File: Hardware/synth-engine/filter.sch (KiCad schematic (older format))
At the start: 36 parts, among them J6 AUDIO-JACK4-.25-HORIZ-TRS, U4 TL074CN, U5 SSI2144

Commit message: add separate PCB with potentiometers and switches and connector between control board and synth engine
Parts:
- U4: footprint SparkFun-AnalogIC:SOIC8 -> SparkFun-AnalogIC:SO16
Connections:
- net at J6.RING (RING-NORM): now also J6.TIP, RV17.2
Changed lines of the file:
@@
 $Descr A4 11693 8268
 encoding utf-8
-Sheet 4 6
+Sheet 4 7
 Title ""
 Date ""
@@
 F 0 "U4" H 8050 3800 60  0000 L CNN
 F 1 "TL074CN" H 8050 3550 60  0000 L CNN
-F 2 "SparkFun-AnalogIC:SOIC8" H 8150 3900 60  0001 L CNN
+F 2 "SparkFun-AnalogIC:SO16" H 8150 3900 60  0001 L CNN
 F 3 "http://www.ti.com/lit/ds/symlink/tl071a.pdf" H 8150 4000 60  0001 L CNN
 F 4 "296-1777-5-ND" H 8150 4100 60  0001 L CNN "Digi-Key_PN"
@@
 F 0 "U4" H 3900 4400 60  0000 L CNN
 F 1 "TL074CN" H 3900 4150 60  0000 L CNN
-F 2 "SparkFun-AnalogIC:SOIC8" H 4000 4500 60  0001 L CNN
+F 2 "SparkFun-AnalogIC:SO16" H 4000 4500 60  0001 L CNN
 F 3 "http://www.ti.com/lit/ds/symlink/tl071a.pdf" H 4000 4600 60  0001 L CNN
 F 4 "296-1777-5-ND" H 4000 4700 60  0001 L CNN "Digi-Key_PN"

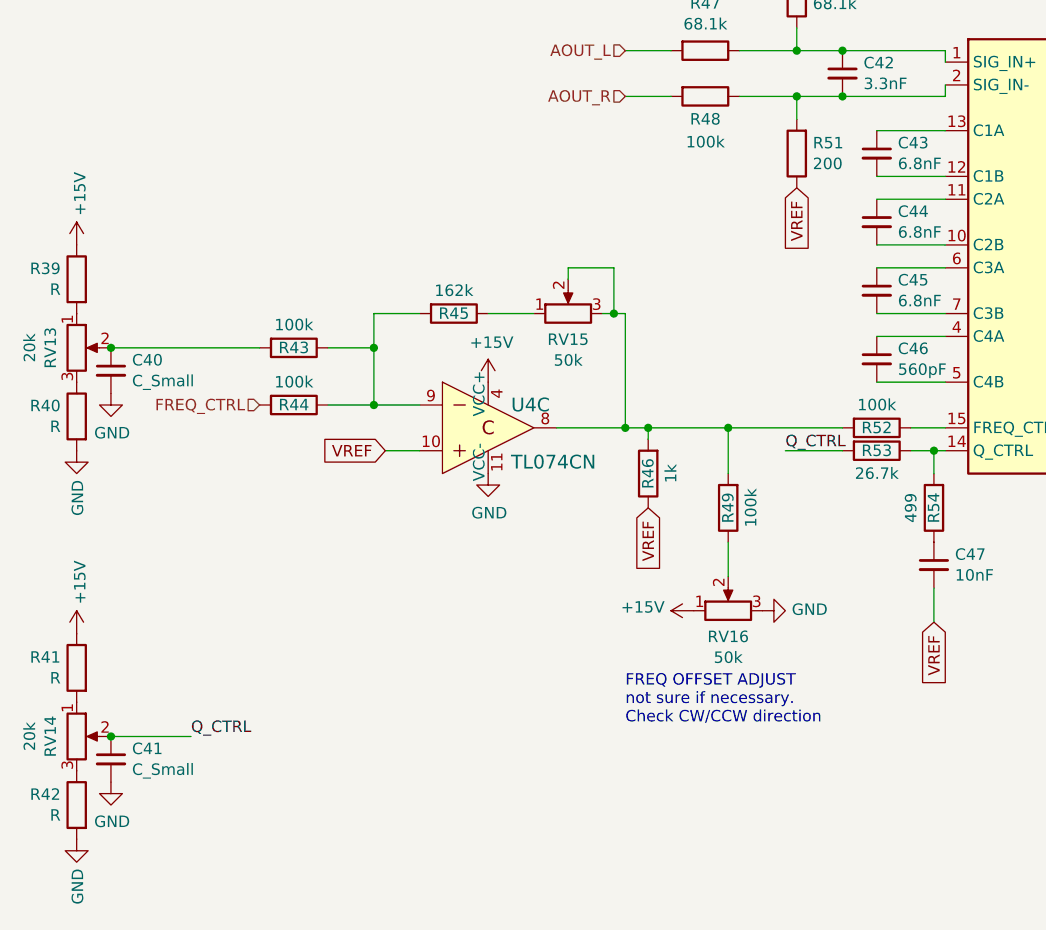
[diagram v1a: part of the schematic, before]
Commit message: initial routing complete. Still need to do ground plane pours. There are still some issues with incorrect footprints.
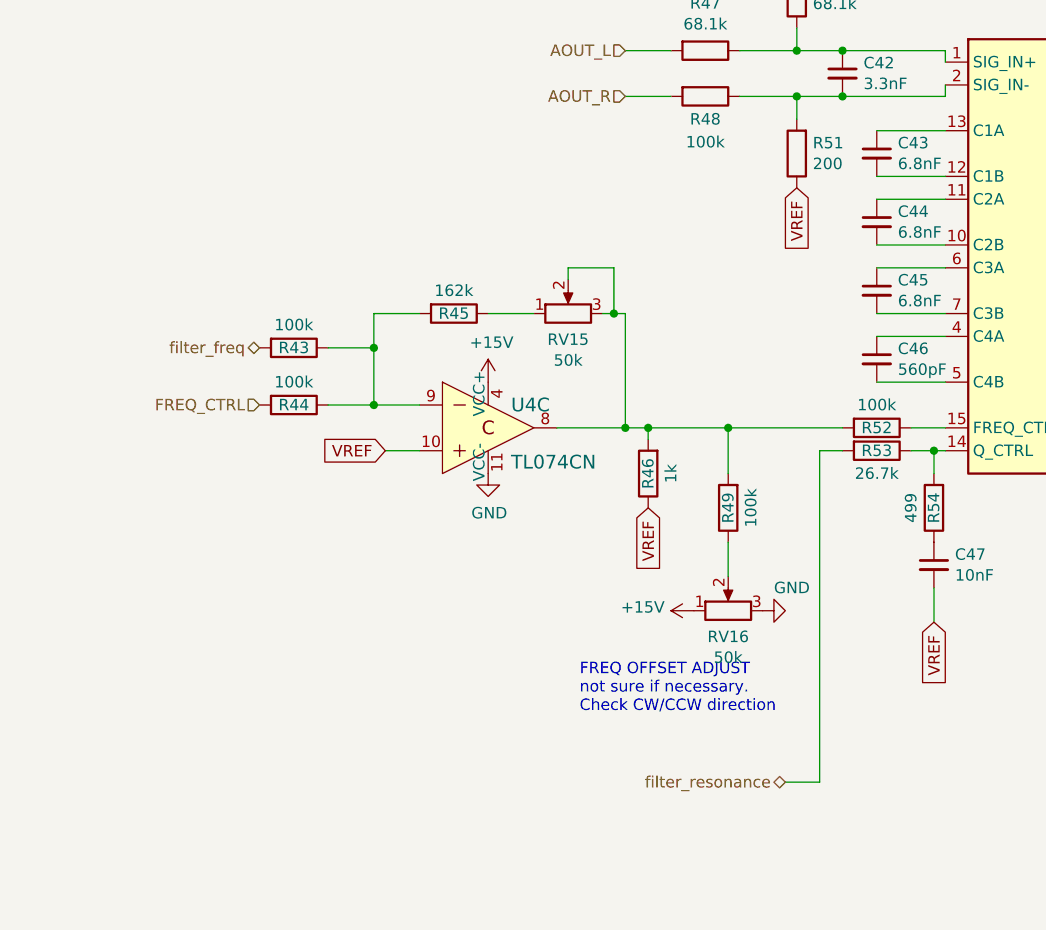
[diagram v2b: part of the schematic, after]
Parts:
- removed C40, C41: C_Small, SparkFun-Passives:0805, symbol Device:C_Small
- removed R39, R40, R41, R42: R, SparkFun-Passives:0805, symbol Device:R
- removed RV13, RV14: 20k, Potentiometer_THT:Potentiometer_Alps_RK09K_Single_Vertical, symbol Device:R_POT
- RV15, RV16: footprint Potentiometer_THT:Potentiometer_Alps_RK09K_Single_Vertical -> SparkFun-Electromechanical:TRIMPOT-3MM-2
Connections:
- net filter_freq: now reaches R43.2
- net at J6.RING (RING-NORM): now also J6.TIP, RV17.2
- net Q_CTRL renamed filter_resonance
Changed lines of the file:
@@
 P 5000 5100
 F 0 "#PWR069" H 5000 4850 50  0001 C CNN
-F 1 "GND" V 5005 4972 50  0000 R CNN
+F 1 "GND" V 5100 5050 50  0000 R CNN
 F 2 "" H 5000 5100 50  0001 C CNN
 F 3 "" H 5000 5100 50  0001 C CNN
@@
 	0    -1   -1   0
 $EndComp
-Text Notes 4400 5600 0    50   ~ 0
+Text Notes 4200 5550 0    50   ~ 0
 FREQ OFFSET ADJUST\nnot sure if necessary.\nCheck CW/CCW direction
 $Comp
@@
 F 0 "RV16" V 4736 5100 50  0000 C CNN
 F 1 "50k" V 4645 5100 50  0000 C CNN
-F 2 "Potentiometer_THT:Potentiometer_Alps_RK09K_Single_Vertical" H 4850 5100 50  0001 C CNN
+F 2 "SparkFun-Electromechanical:TRIMPOT-3MM-2" H 4850 5100 50  0001 C CNN
 F 3 "~" H 4850 5100 50  0001 C CNN
 	1    4850 5100
@@
 F 0 "RV15" V 4036 3800 50  0000 C CNN
 F 1 "50k" V 3945 3800 50  0000 C CNN
-F 2 "Potentiometer_THT:Potentiometer_Alps_RK09K_Single_Vertical" H 4150 3800 50  0001 C CNN
+F 2 "SparkFun-Electromechanical:TRIMPOT-3MM-2" H 4150 3800 50  0001 C CNN
 F 3 "~" H 4150 3800 50  0001 C CNN
 	1    4150 3800
@@
 	1    0    0    -1
 $EndComp
-Text Label 5100 4400 0    50   ~ 0
-Q_CTRL
-Wire Wire Line
-	5100 4400 5350 4400
 Text GLabel 5750 5150 3    50   Input ~ 0
 VREF
@@
 $EndComp
 $Comp
-L power:+15V #PWR060
-U 1 1 5DDC8B0C
-P 2000 3500
-F 0 "#PWR060" H 2000 3350 50  0001 C CNN
-F 1 "+15V" V 2015 3628 50  0000 L CNN
-F 2 "" H 2000 3500 50  0001 C CNN
-F 3 "" H 2000 3500 50  0001 C CNN
-	1    2000 3500
-	1    0    0    -1
-$EndComp
-$Comp
-L power:GND #PWR061
-U 1 1 5DDC8B12
-P 2000 4400
-F 0 "#PWR061" H 2000 4150 50  0001 C CNN
-F 1 "GND" V 2005 4272 50  0000 R CNN
-F 2 "" H 2000 4400 50  0001 C CNN
-F 3 "" H 2000 4400 50  0001 C CNN
-	1    2000 4400
-	1    0    0    -1
-$EndComp
-$Comp
-L Device:R_POT RV13
-U 1 1 5DDC8B18
-P 2000 3950
-F 0 "RV13" V 1886 3950 50  0000 C CNN
-F 1 "20k" V 1795 3950 50  0000 C CNN
-F 2 "Potentiometer_THT:Potentiometer_Alps_RK09K_Single_Vertical" H 2000 3950 50  0001 C CNN
-F 3 "~" H 2000 3950 50  0001 C CNN
-	1    2000 3950
-	1    0    0    -1
-$EndComp
-Wire Wire Line
-	2150 3950 2800 3950
-$Comp
-L Device:R R40
-U 1 1 5DDD4D4F
-P 2000 4250
-F 0 "R40" H 2070 4296 50  0000 L CNN
-F 1 "R" H 2070 4205 50  0000 L CNN
-F 2 "SparkFun-Passives:0805" V 1930 4250 50  0001 C CNN
-F 3 "~" H 2000 4250 50  0001 C CNN
-	1    2000 4250
-	-1   0    0    -1
-$EndComp
-$Comp
-L Device:R R39
-U 1 1 5DDD7C21
-P 2000 3650
-F 0 "R39" H 2070 3696 50  0000 L CNN
-F 1 "R" H 2070 3605 50  0000 L CNN
-F 2 "SparkFun-Passives:0805" V 1930 3650 50  0001 C CNN
-F 3 "~" H 2000 3650 50  0001 C CNN
-	1    2000 3650
-	-1   0    0    -1
-$EndComp
-$Comp
-L Device:C_Small C40
-U 1 1 5DDDB3D4
-P 2150 4050
-F 0 "C40" H 2242 4096 50  0000 L CNN
-F 1 "C_Small" H 2242 4005 50  0000 L CNN
-F 2 "SparkFun-Passives:0805" H 2150 4050 50  0001 C CNN
-F 3 "~" H 2150 4050 50  0001 C CNN
-	1    2150 4050
-	1    0    0    -1
-$EndComp
-Connection ~ 2150 3950
-$Comp
-L power:GND #PWR064
-U 1 1 5DDDB4EF
-P 2150 4150
-F 0 "#PWR064" H 2150 3900 50  0001 C CNN
-F 1 "GND" H 2155 3977 50  0000 C CNN
-F 2 "" H 2150 4150 50  0001 C CNN
-F 3 "" H 2150 4150 50  0001 C CNN
-	1    2150 4150
-	1    0    0    -1
-$EndComp
-$Comp
-L power:+15V #PWR062
-U 1 1 5DDE1C9A
-P 2000 5200
-F 0 "#PWR062" H 2000 5050 50  0001 C CNN
-F 1 "+15V" V 2015 5328 50  0000 L CNN
-F 2 "" H 2000 5200 50  0001 C CNN
-F 3 "" H 2000 5200 50  0001 C CNN
-	1    2000 5200
-	1    0    0    -1
-$EndComp
-$Comp
-L power:GND #PWR063
-U 1 1 5DDE1CA0
-P 2000 6100
-F 0 "#PWR063" H 2000 5850 50  0001 C CNN
-F 1 "GND" V 2005 5972 50  0000 R CNN
-F 2 "" H 2000 6100 50  0001 C CNN
-F 3 "" H 2000 6100 50  0001 C CNN
-	1    2000 6100
-	1    0    0    -1
-$EndComp
-$Comp
-L Device:R_POT RV14
-U 1 1 5DDE1CA6
-P 2000 5650
-F 0 "RV14" V 1886 5650 50  0000 C CNN
-F 1 "20k" V 1795 5650 50  0000 C CNN
-F 2 "Potentiometer_THT:Potentiometer_Alps_RK09K_Single_Vertical" H 2000 5650 50  0001 C CNN
-F 3 "~" H 2000 5650 50  0001 C CNN
-	1    2000 5650
-	1    0    0    -1
-$EndComp
-Wire Wire Line
-	2150 5650 2500 5650
-$Comp
-L Device:R R42
-U 1 1 5DDE1CAD
-P 2000 5950
-F 0 "R42" H 2070 5996 50  0000 L CNN
-F 1 "R" H 2070 5905 50  0000 L CNN
-F 2 "SparkFun-Passives:0805" V 1930 5950 50  0001 C CNN
-F 3 "~" H 2000 5950 50  0001 C CNN
-	1    2000 5950
-	-1   0    0    -1
-$EndComp
-$Comp
-L Device:R R41
-U 1 1 5DDE1CB3
-P 2000 5350
-F 0 "R41" H 2070 5396 50  0000 L CNN
-F 1 "R" H 2070 5305 50  0000 L CNN
-F 2 "SparkFun-Passives:0805" V 1930 5350 50  0001 C CNN
-F 3 "~" H 2000 5350 50  0001 C CNN
-	1    2000 5350
-	-1   0    0    -1
-$EndComp
-$Comp
-L Device:C_Small C41
-U 1 1 5DDE1CB9
-P 2150 5750
-F 0 "C41" H 2242 5796 50  0000 L CNN
-F 1 "C_Small" H 2242 5705 50  0000 L CNN
-F 2 "SparkFun-Passives:0805" H 2150 5750 50  0001 C CNN
-F 3 "~" H 2150 5750 50  0001 C CNN
-	1    2150 5750
-	1    0    0    -1
-$EndComp
-Connection ~ 2150 5650
-$Comp
-L power:GND #PWR065
-U 1 1 5DDE1CC0
-P 2150 5850
-F 0 "#PWR065" H 2150 5600 50  0001 C CNN
-F 1 "GND" H 2155 5677 50  0000 C CNN
-F 2 "" H 2150 5850 50  0001 C CNN
-F 3 "" H 2150 5850 50  0001 C CNN
-	1    2150 5850
-	1    0    0    -1
-$EndComp
-Text Label 2500 5650 0    50   ~ 0
-Q_CTRL
-$Comp
 L Device:R R51
 U 1 1 5DE8132C
@@
 Text HLabel 2800 4200 0    50   Input ~ 0
 FREQ_CTRL
+Text HLabel 2800 3950 0    50   BiDi ~ 0
+filter_freq
+Text HLabel 5100 5850 0    50   BiDi ~ 0
+filter_resonance
+Wire Wire Line
+	5250 4400 5250 5850
+Wire Wire Line
+	5250 5850 5100 5850
+Wire Wire Line
+	5250 4400 5350 4400
 $EndSCHEMATC

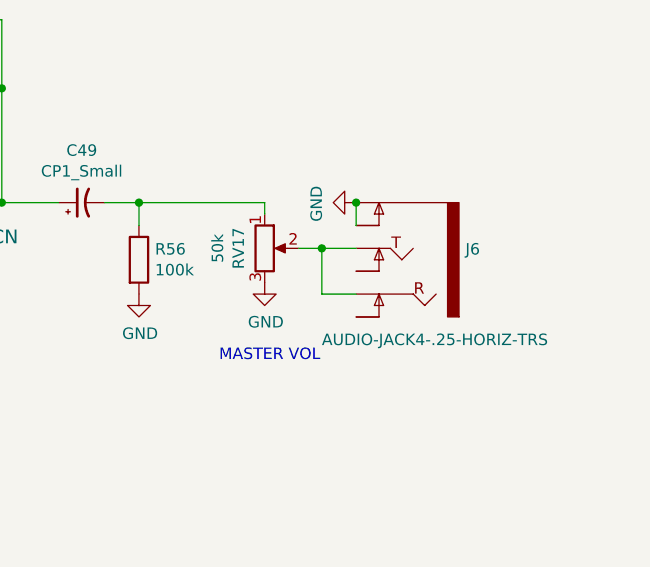
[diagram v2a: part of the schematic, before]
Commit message: fix some footprint errors
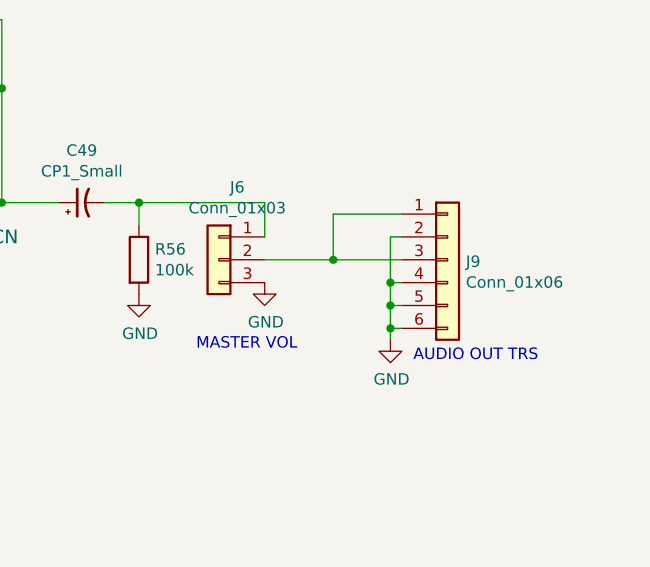
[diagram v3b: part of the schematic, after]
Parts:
- removed J6: AUDIO-JACK4-.25-HORIZ-TRS, SparkFun-Connectors:AUDIO-JACK-.25-INCH-HORIZ-PTH, symbol SparkFun-Connectors:AUDIO-JACK4-.25-HORIZ-TRS
- removed RV17: 50k, Potentiometer_THT:Potentiometer_Alps_RK09K_Single_Vertical, symbol Device:R_POT
- added J6: Conn_01x03, SparkFun-Connectors:1X03, symbol Connector_Generic:Conn_01x03
- added J9: Conn_01x06, SparkFun-Connectors:1X06, symbol Connector_Generic:Conn_01x06
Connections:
- net GND: now also J6.3 (Pin_3), J9.2 (Pin_2), J9.4 (Pin_4), J9.5 (Pin_5), J9.6 (Pin_6)
- net at C49.2, R56.1: now also J6.1 (Pin_1)
- new net: J6.2 (Pin_2), J9.1 (Pin_1), J9.3 (Pin_3)
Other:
- note added: "AUDIO OUT TRS"
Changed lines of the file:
@@
 Wire Wire Line
 	5150 2650 5350 2650
-$Comp
-L SparkFun-Connectors:AUDIO-JACK4-.25-HORIZ-TRS J6
-U 1 1 5DE9AC5B
-P 10100 4000
-F 0 "J6" H 9822 4096 50  0000 R CNN
-F 1 "AUDIO-JACK4-.25-HORIZ-TRS" H 10450 3700 50  0000 R CNN
-F 2 "SparkFun-Connectors:AUDIO-JACK-.25-INCH-HORIZ-PTH" H 10130 4150 20  0001 C CNN
-F 3 "" H 10100 4000 60  0000 C CNN
-	1    10100 4000
-	-1   0    0    -1
-$EndComp
-$Comp
-L power:GND #PWR076
-U 1 1 5DE9C6F0
-P 9900 3700
-F 0 "#PWR076" H 9900 3450 50  0001 C CNN
-F 1 "GND" H 9905 3527 50  0000 C CNN
-F 2 "" H 9900 3700 50  0001 C CNN
-F 3 "" H 9900 3700 50  0001 C CNN
-	1    9900 3700
-	0    1    1    0
-$EndComp
-Wire Wire Line
-	9900 3800 9900 3700
-Connection ~ 9900 3700
-$Comp
-L Device:R_POT RV17
-U 1 1 5DEA599F
-P 9500 3900
-F 0 "RV17" V 9386 3900 50  0000 C CNN
-F 1 "50k" V 9295 3900 50  0000 C CNN
-F 2 "Potentiometer_THT:Potentiometer_Alps_RK09K_Single_Vertical" H 9500 3900 50  0001 C CNN
-F 3 "~" H 9500 3900 50  0001 C CNN
-	1    9500 3900
-	1    0    0    -1
-$EndComp
-Wire Wire Line
-	9500 3750 9500 3700
 Wire Wire Line
 	9500 3700 8950 3700
@@
 	1    0    0    -1
 $EndComp
-Wire Wire Line
-	9900 3900 9750 3900
-Wire Wire Line
-	9750 3900 9750 4100
-Wire Wire Line
-	9750 4100 9900 4100
-Connection ~ 9750 3900
-Wire Wire Line
-	9750 3900 9650 3900
-Text Notes 9300 4400 0    50   ~ 0
+Text Notes 9200 4350 0    50   ~ 0
 MASTER VOL
 Text HLabel 2800 4200 0    50   Input ~ 0
@@
 Wire Wire Line
 	5250 4400 5350 4400
+$Comp
+L Connector_Generic:Conn_01x06 J9
+U 1 1 5DE609DC
+P 10300 3950
+F 0 "J9" H 10380 3942 50  0000 L CNN
+F 1 "Conn_01x06" H 10380 3851 50  0000 L CNN
+F 2 "SparkFun-Connectors:1X06" H 10300 3950 50  0001 C CNN
+F 3 "~" H 10300 3950 50  0001 C CNN
+	1    10300 3950
+	1    0    0    -1
+$EndComp
+$Comp
+L power:GND #PWR0123
+U 1 1 5DE61520
+P 10050 4300
+F 0 "#PWR0123" H 10050 4050 50  0001 C CNN
+F 1 "GND" H 10055 4127 50  0000 C CNN
+F 2 "" H 10050 4300 50  0001 C CNN
+F 3 "" H 10050 4300 50  0001 C CNN
+	1    10050 4300
+	1    0    0    -1
+$EndComp
+Wire Wire Line
+	10050 4300 10050 4250
+Wire Wire Line
+	10050 4250 10100 4250
+Wire Wire Line
+	10100 4150 10050 4150
+Wire Wire Line
+	10050 4150 10050 4250
+Connection ~ 10050 4250
+Wire Wire Line
+	9800 3950 9800 3750
+Wire Wire Line
+	9800 3750 10100 3750
+Wire Wire Line
+	9800 3950 10100 3950
+Connection ~ 9800 3950
+Wire Wire Line
+	10100 3850 10050 3850
+Wire Wire Line
+	10050 3850 10050 4050
+Connection ~ 10050 4150
+Wire Wire Line
+	10100 4050 10050 4050
+Connection ~ 10050 4050
+Wire Wire Line
+	10050 4050 10050 4150
+$Comp
+L Connector_Generic:Conn_01x03 J6
+U 1 1 5DE6BE76
+P 9300 3950
+F 0 "J6" H 9220 4267 50  0000 C CNN
+F 1 "Conn_01x03" H 9220 4176 50  0000 C CNN
+F 2 "SparkFun-Connectors:1X03" H 9300 3950 50  0001 C CNN
+F 3 "~" H 9300 3950 50  0001 C CNN
+	1    9300 3950
+	-1   0    0    -1
+$EndComp
+Wire Wire Line
+	9500 3700 9500 3850
+Wire Wire Line
+	9500 3950 9800 3950
+Text Notes 10150 4400 0    50   ~ 0
+AUDIO OUT TRS
 $EndSCHEMATC
